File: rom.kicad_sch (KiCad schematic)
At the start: 5 parts, among them IC17 27C256, IC18 74LS08

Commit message: move to samx4
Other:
- company: (none) -> Dragon Data
- title: (none) -> Dragon 32 CPU UK PAL
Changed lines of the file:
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@@
   (paper "A3")
   (title_block
+    (title "Dragon 32 CPU UK PAL")
     (date "2023-05-25")
     (rev "3.0")
-    (comment 2 "Reposition dram and buffer")
+    (company "Dragon Data")
+    (comment 1 "Modified by Julian Brown")
+    (comment 2 "SAMx4 by Ciaran Anscomb")
   )
   (no_connect (at 378.714 167.386))

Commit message: rework board
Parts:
- removed IC17: 27C256, Package_DIP:DIP-28_W15.24mm, symbol Memory_EPROM:27C256
- removed JP1: SELECT ROM, Connector_PinHeader_2.54mm:PinHeader_1x03_P2.54mm_Vertical, symbol Jumper:Jumper_3_Bridged12
- removed JP7: 27C512, Jumper:SolderJumper-3_P1.3mm_Open_Pad1.0x1.5mm, symbol Jumper:SolderJumper_3_Open
- added U8: 28C256, Package_LCC:PLCC-32_THT-Socket, symbol BenEater:28C256_PLCC
- IC18: value 74LS08 -> 74ACT08; footprint Package_DIP:DIP-14_W7.62mm -> Package_SO:SOIC-14_3.9x8.7mm_P1.27mm; DigiKey (none) -> MC74ACT08DR2GOSCT-ND
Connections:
- net +5V: now also U8.31 (~{WE}), U8.32 (VCC)
- net A0: now also U8.11 (A0)
- net A1: now also U8.10 (A1)
- net A10: now also U8.24 (A10)
- net A11: now also U8.27 (A11)
- net A12: now also U8.3 (A12)
- net A13: now also U8.30 (A13)
- net A2: now also U8.9 (A2)
- net A3: now also U8.8 (A3)
- net A4: now also U8.7 (A4)
- net A5: now also U8.6 (A5)
- net A6: now also U8.5 (A6)
- net A7: now also U8.4 (A7)
- net A8: now also U8.29 (A8)
- net A9: now also U8.28 (A9)
- net D0: now also U8.13 (D0)
- net D1: now also U8.14 (D1)
- net D2: now also U8.15 (D2)
- net D3: now also U8.18 (D3)
- net D4: now also U8.19 (D4)
- net D5: now also U8.20 (D5)
- net D6: now also U8.21 (D6)
- net D7: now also U8.22 (D7)
- net GND: now also U8.16 (GND)
- net ~{ROM}: now also U8.23 (~{CS}), U8.25 (~{OE})
- net at JP6.4 (Out): now also U8.2 (A14)

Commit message: serial wiring
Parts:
- removed IC18: 74ACT08, Package_SO:SOIC-14_3.9x8.7mm_P1.27mm, symbol 74xx:74LS08
- added U9: 74HCT1G08, Package_TO_SOT_SMD:SOT-353_SC-70-5_Handsoldering, symbol vdg:74HC1G08
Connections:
- net +5V: now also U9.5 (Vcc)
- net GND: now also U9.3 (Gnd)
- net ~{E17}: now also U9.2 (IN_A)
- net ~{E18}: now also U9.1 (IN_B)
- net ~{ROM}: now also U9.4 (OUT_Y)
- no-connect marks 9 -> 0

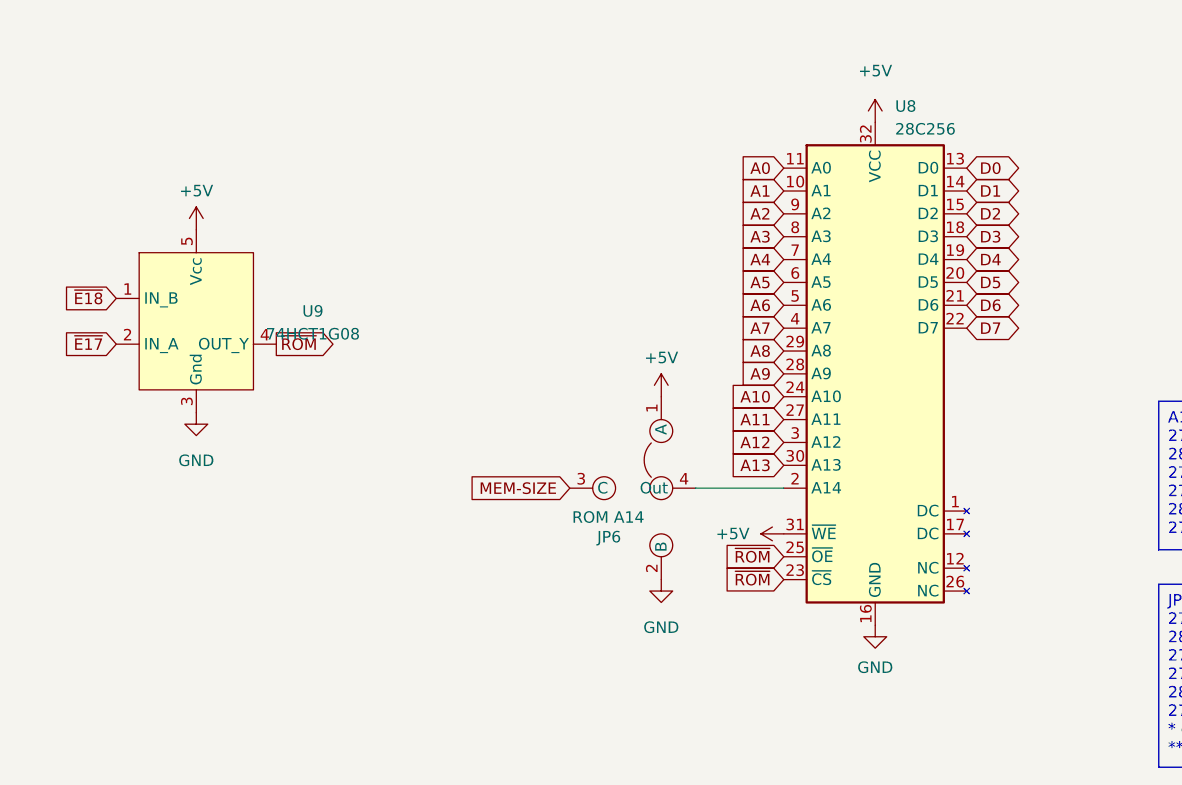
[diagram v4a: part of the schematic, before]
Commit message: switch to fpga
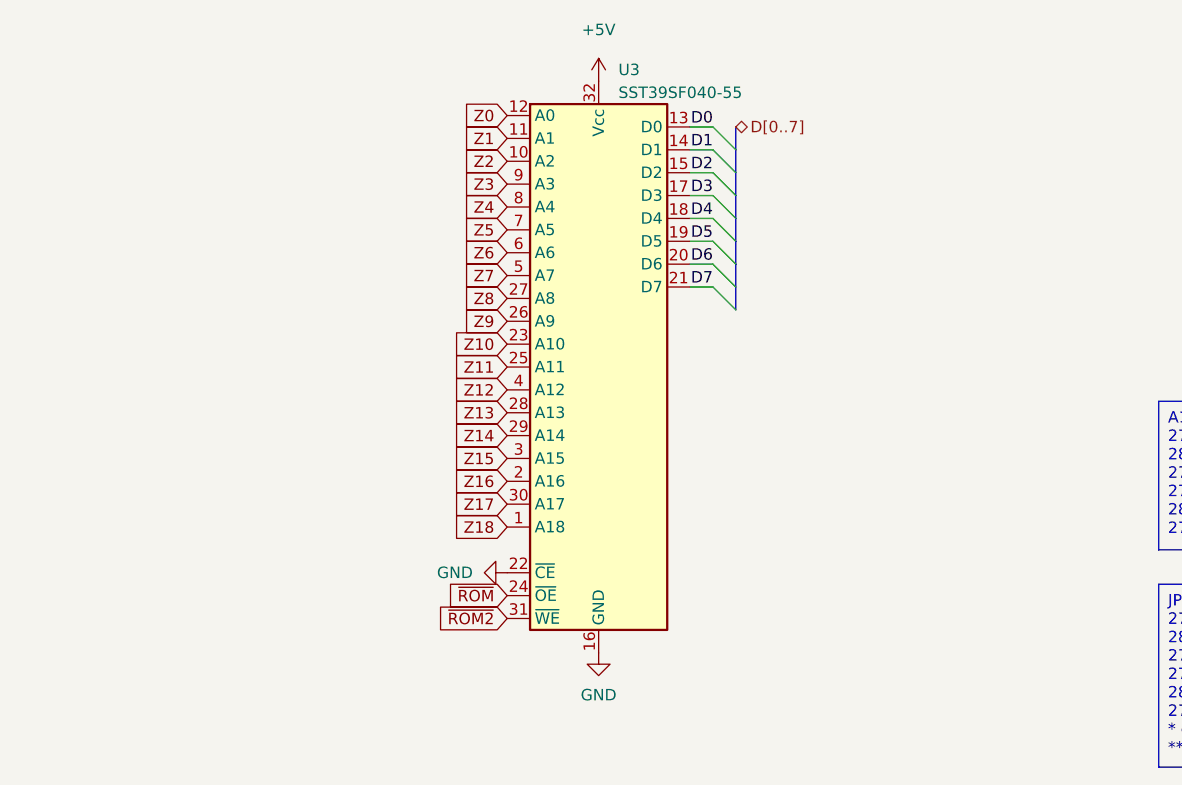
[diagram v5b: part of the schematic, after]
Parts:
- removed JP6: ROM A14, Dragon:Jumper_4, symbol vdg:Jumper_4
- removed U8: 28C256, Package_LCC:PLCC-32_THT-Socket, symbol BenEater:28C256_PLCC
- removed U9: 74HCT1G08, Package_TO_SOT_SMD:SOT-353_SC-70-5_Handsoldering, symbol vdg:74HC1G08
- added U3: SST39SF040-55, Package_LCC:PLCC-32_THT-Socket, symbol Motorola PIA:29C040
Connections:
- net +5V: now also U3.32 (Vcc)
- net D0: now also U3.13 (D0)
- net D1: now also U3.14 (D1)
- net D2: now also U3.15 (D2)
- net D3: now also U3.17 (D3)
- net D4: now also U3.18 (D4)
- net D5: now also U3.19 (D5)
- net D6: now also U3.20 (D6)
- net D7: now also U3.21 (D7)
- net GND: now also U3.16 (GND), U3.22 (~{CE})
- net ~{ROM}: now also U3.24 (~{OE})
- new net Z0: U3.12 (A0)
- new net Z1: U3.11 (A1)
- new net Z10: U3.23 (A10)
- new net Z11: U3.25 (A11)
- new net Z12: U3.4 (A12)
- new net Z13: U3.28 (A13)
- new net Z14: U3.29 (A14)
- new net Z15: U3.3 (A15)
- new net Z16: U3.2 (A16)
- new net Z17: U3.30 (A17)
- new net Z18: U3.1 (A18)
- new net Z2: U3.10 (A2)
- new net Z3: U3.9 (A3)
- new net Z4: U3.8 (A4)
- new net Z5: U3.7 (A5)
- new net Z6: U3.6 (A6)
- new net Z7: U3.5 (A7)
- new net Z8: U3.27 (A8)
- new net Z9: U3.26 (A9)
- new net ~{ROM2}: U3.31 (~{WE})
